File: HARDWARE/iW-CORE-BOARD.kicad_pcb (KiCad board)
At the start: 4 copper layers, 118 x 80 mm, 121 parts, among them J1 Conn_01x40_MountingPin, J2 Conn_01x06_MountingPin, J3 1746142-1, J4 Conn_02x09_Counter_Clockwise, J5 Conn_02x09_Counter_Clockwise, J6 Conn_02x05_Odd_Even, J7 USB_C_Receptacle_USB2.0, J8 Conn_02x05_Odd_Even, J9 USB_C_Receptacle_USB2.0, P1 ST-TF-003A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

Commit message: att.
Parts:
- moved JP1 163.7 mm to (96.0, 77.5)
- moved C41 162.5 mm to (100.0, 86.5)
- moved JP2 161.6 mm to (96.0, 81.5)
- moved C38 158.3 mm to (99.8, 77.2)
- moved C39 156.5 mm to (106.0, 90.0), turned to 90 degrees
- moved C40 154.6 mm to (108.0, 90.0), turned to 90 degrees
- moved C42 153.1 mm to (109.5, 86.2), turned to 90 degrees
- moved L2 148.8 mm to (103.5, 79.5)
- moved R46 143.8 mm to (100.1, 84.5)
- moved U12 140.2 mm to (105.8, 85.6), turned to 90 degrees
- moved R47 140.1 mm to (102.8, 86.0), turned to 90 degrees
- moved FB3 139.9 mm to (99.5, 79.5)
- moved R48 128.9 mm to (110.5, 100.0), turned to -90 degrees
- moved FB2 127.8 mm to (109.8, 90.0), turned to 90 degrees
- moved C50 126.6 mm to (108.5, 104.0), turned to -90 degrees
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
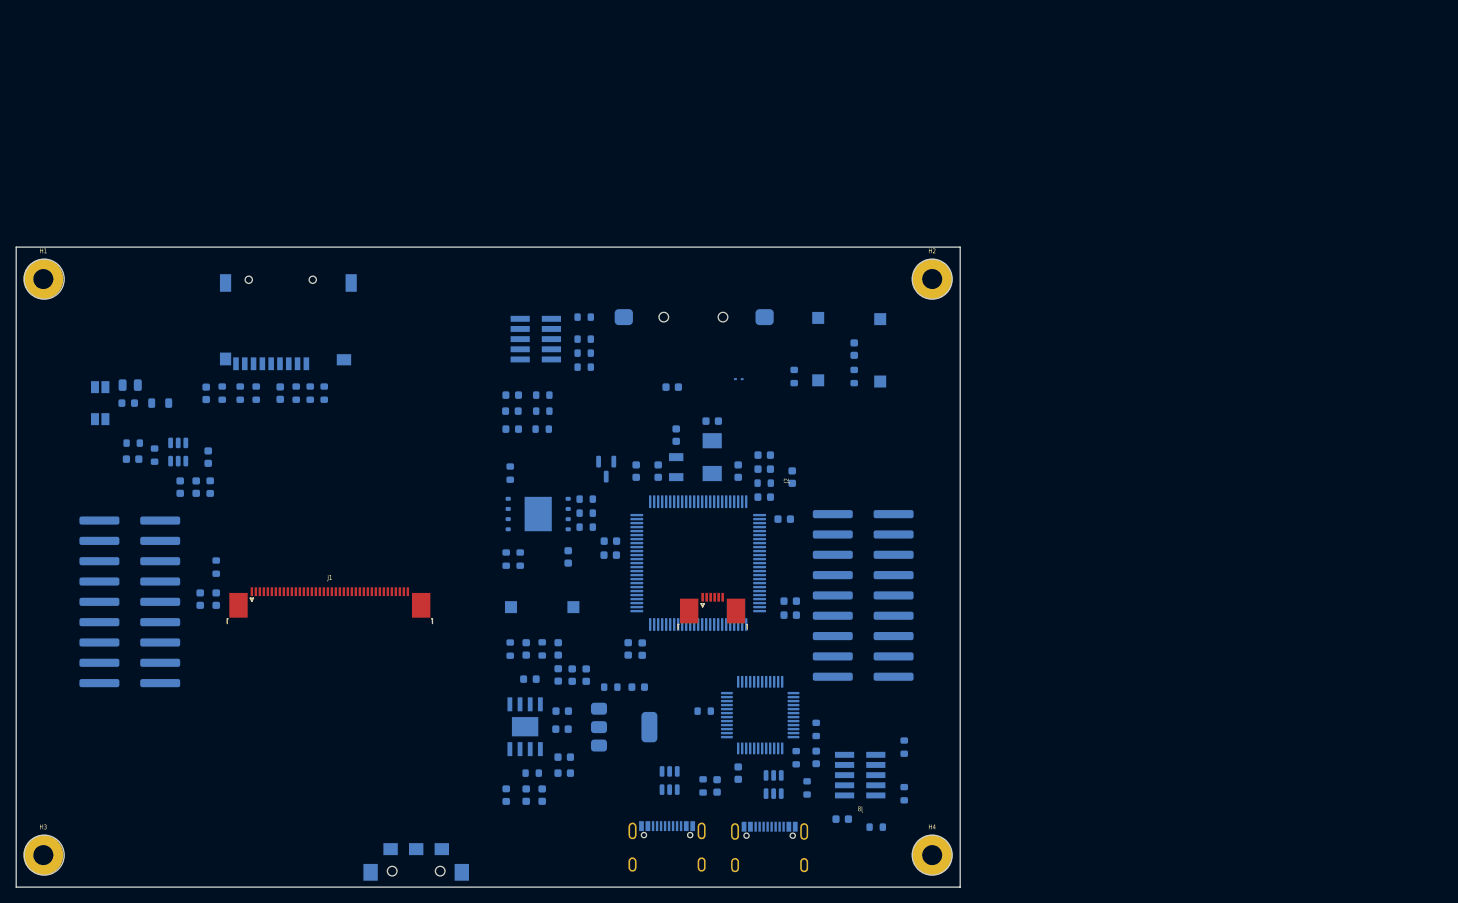
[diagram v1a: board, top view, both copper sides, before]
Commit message: Fix componentes possiton
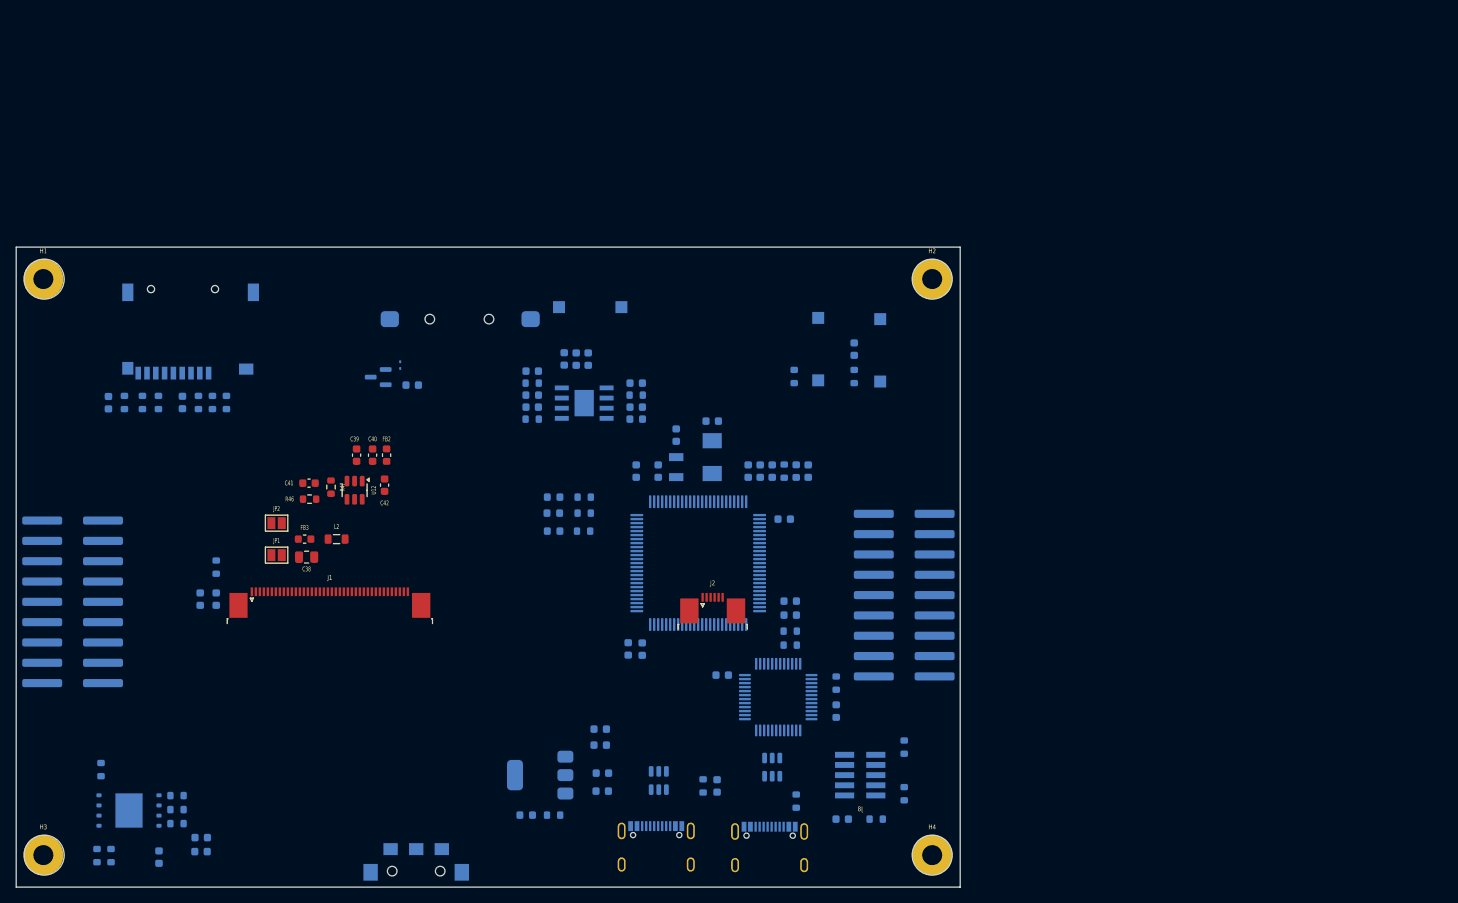
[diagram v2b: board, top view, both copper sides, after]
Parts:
- removed J6: Conn_02x05_Odd_Even, Connector_PinHeader_1.27mm:PinHeader_2x05_P1.27mm_Vertical_SMD
- removed R34, R35, R36, R37: 22R, Resistor_SMD:R_0603_1608Metric
- C38, C39, C40, C41, C42, FB2, FB3, JP1, JP2, L2, R46, R47, U12: moved to F.Cu
- moved C36 63.4 mm to (103.3, 136.2)
- moved U7 63.2 mm to (99.6, 130.4)
- moved C1 63.2 mm to (108.6, 135.6)
- moved C4 63.2 mm to (108.6, 133.8)
- moved R28 63.2 mm to (105.6, 128.6)
- moved R29 63.2 mm to (96.1, 125.3)
- moved R30 63.2 mm to (95.6, 136.1)
- moved R31 63.2 mm to (105.6, 132.1)
- moved R32 63.2 mm to (105.6, 130.3)
- moved R33 63.2 mm to (97.3, 136.1)
- moved C18 52.8 mm to (163.0, 77.0), turned to 0 degrees
- moved C17 50.4 mm to (163.0, 80.0), turned to 0 degrees
- moved D1 49.7 mm to (163.0, 81.5), turned to 180 degrees
- moved R9 49.0 mm to (163.0, 78.5), turned to 0 degrees
- moved D7 42.4 mm to (133.5, 74.8), turned to -90 degrees
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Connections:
- J9 pad A6: USB_OB_P -> /JTAG/USB_O_P
- J9 pad A7: USB_OB_N -> /JTAG/USB_O_N
- J9 pad B6: USB_OB_P -> /JTAG/USB_O_P
- J9 pad B7: USB_OB_N -> /JTAG/USB_O_N
- U11 pad 1: USB_OB_N -> /JTAG/USB_O_N
- U11 pad 3: USB_OB_P -> /JTAG/USB_O_P

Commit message: esa
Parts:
- added C35: 0.1uF, Capacitor_SMD:C_0603_1608Metric, B.Cu at (177.7, 124.4)
- added C51: 0.1uF, Capacitor_SMD:C_0603_1608Metric, B.Cu at (172.4, 113.2)
- added C52: 0.1uF, Capacitor_SMD:C_0603_1608Metric, B.Cu at (181.4, 107.7)
- added REF**: BL-5C, Battery:BL-5C, B.Cu at (145.5, 132.9)
- C19, C20, C21: footprint Capacitor_SMD:C_0603_1608Metric -> Capacitor_SMD:C_1206_3216Metric
- C36, R28, R29, R30, R31, R32, R33, R49, U7: moved to F.Cu
- J4, J5: footprint Connector_IDC:IDC-Header_2x09_P2.54mm_Vertical_SMD -> Connector_PinSocket_2.54mm:PinSocket_2x09_P2.54mm_Vertical_SMD
- L1: footprint Inductor_SMD:L_0603_1608Metric -> Inductor_SMD:L_APV_ANR6020
- R38: value 100R -> 0R; footprint Resistor_SMD:R_0603_1608Metric -> Resistor_SMD:R_1206_3216Metric
- moved C44 86.8 mm to (181.6, 44.3)
- moved C45 86.8 mm to (181.3, 38.5)
- moved C46 86.8 mm to (181.3, 36.5)
- moved D10 86.8 mm to (172.1, 47.3)
- moved U9 86.8 mm to (173.8, 42.3)
- moved C43 86.8 mm to (181.6, 42.0)
- moved R45 86.8 mm to (175.5, 47.3)
- moved D4 73.8 mm to (159.7, 49.8)
- moved R51 73.8 mm to (159.7, 46.3)
- moved C36 63.5 mm to (159.3, 106.2), turned to 180 degrees
- moved C23 62.3 mm to (153.6, 137.7), turned to 0 degrees
- moved R31 61.7 mm to (163.2, 109.7)
- moved R12 60.7 mm to (150.3, 137.7), turned to 180 degrees
- moved R32 60.6 mm to (163.2, 111.3)
- moved U7 60.2 mm to (156.5, 110.7)
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
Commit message: ada
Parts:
- added D2: SS34, Diode_SMD:D_SMA, B.Cu at (165.4, 116.1)
- added D5: SS34, Diode_SMD:D_SMA, B.Cu at (165.3, 119.8)
- C17, C18, C22: footprint Capacitor_SMD:C_0603_1608Metric -> Capacitor_SMD:C_0805_2012Metric
- L2: footprint Inductor_SMD:L_0805_2012Metric -> Inductor_SMD:L_1210_3225Metric
- moved SW3 106.7 mm to (143.3, 137.6)
- moved D1 98.0 mm to (153.2, 138.8)
- moved C17 92.3 mm to (165.0, 127.9), turned to -90 degrees
- moved R11 92.0 mm to (156.7, 130.9), turned to 0 degrees
- moved R9 89.9 mm to (165.1, 123.8), turned to -90 degrees
- moved C18 89.5 mm to (161.3, 123.2), turned to 180 degrees
- moved C46 86.8 mm to (158.6, 120.3), turned to -90 degrees
- moved C45 85.4 mm to (157.0, 120.3), turned to -90 degrees
- moved C43 82.7 mm to (155.0, 120.3), turned to -90 degrees
- moved C44 81.1 mm to (153.3, 120.3), turned to -90 degrees
- moved R51 79.3 mm to (194.1, 117.7), turned to 180 degrees
- moved C4 78.2 mm to (162.2, 76.8), turned to 90 degrees
- moved D4 77.8 mm to (197.6, 117.8), turned to 0 degrees
- moved U9 73.3 mm to (156.2, 113.5), turned to 90 degrees
- moved R45 72.1 mm to (151.2, 115.1), turned to 90 degrees
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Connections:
- C18 pad 1: +5VBUS -> Net-(D2-K)
- C32 pad 1: +5VBUS -> +5V_USBCOM
- C33 pad 1: +5VBUS -> +5V_USB_JLOB
- J9 pad A4: Net-(J9-VBUS-PadA4) -> +5V_USB_JLOB
- J9 pad A9: Net-(J9-VBUS-PadA4) -> +5V_USB_JLOB
- J9 pad B4: Net-(J9-VBUS-PadA4) -> +5V_USB_JLOB
- J9 pad B9: Net-(J9-VBUS-PadA4) -> +5V_USB_JLOB
- R38 pad 2: +5VBUS -> +5V_USBCOM
- R9 pad 1: +5VBUS -> Net-(D2-K)
- U2 pad 1: +5VBUS -> Net-(D2-K)
